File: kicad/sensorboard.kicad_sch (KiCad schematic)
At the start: 8 parts, among them J5 20021121-00010C4LF, U30 SHT40-AD1B-R2, U31 TMP117MAIDRVT

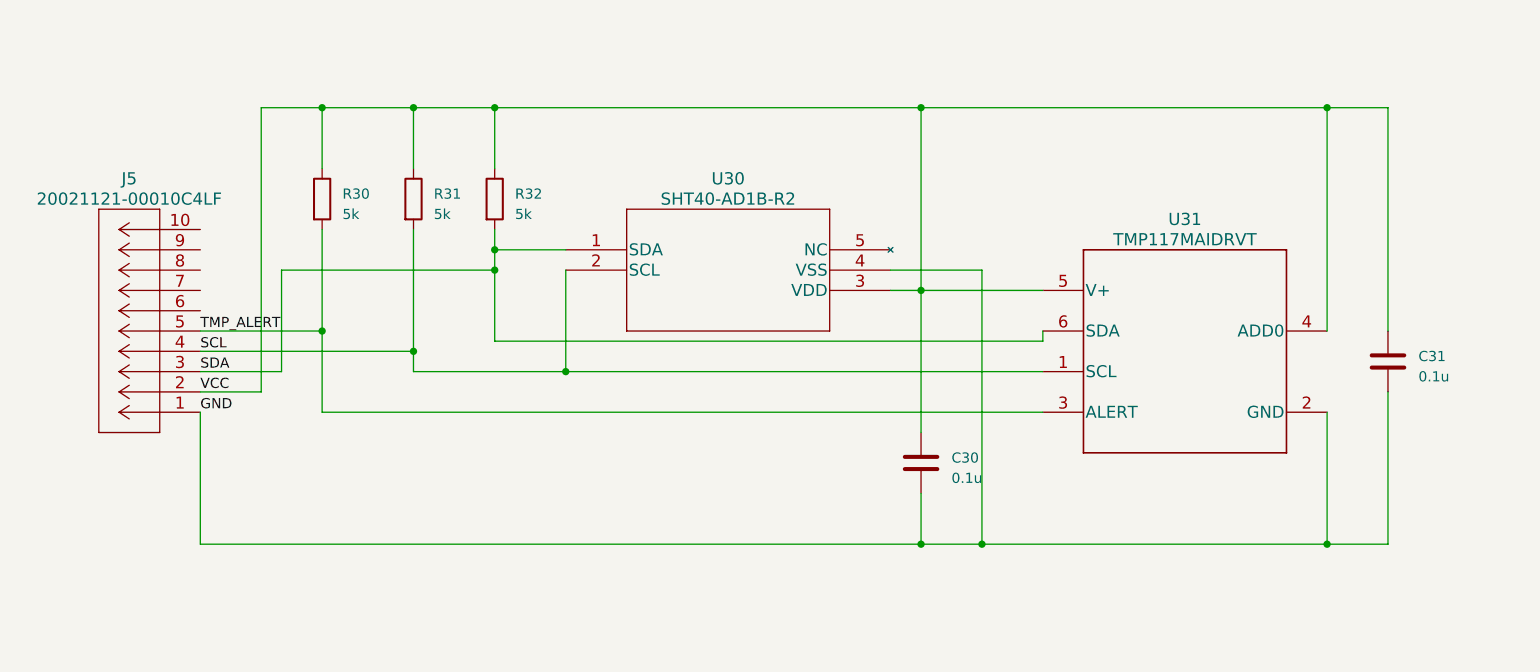
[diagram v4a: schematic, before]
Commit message: schematic editing, led selection
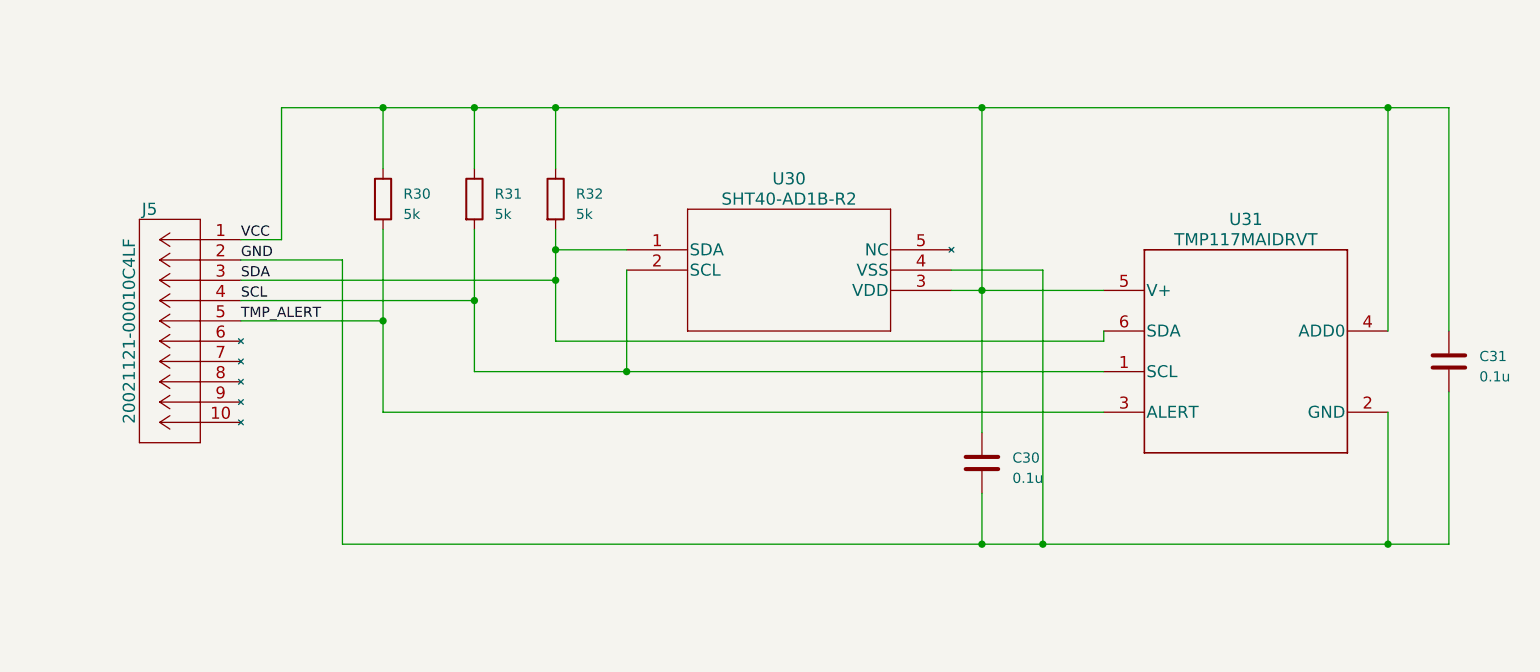
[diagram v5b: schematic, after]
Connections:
- net GND: now also J5.2; no longer J5.1
- net VCC: now also J5.1; no longer J5.2
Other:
- moved on the sheet: C30, C31, R30, R31, R32, U30, U31

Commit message: added footprints and Digikey codes
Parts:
- C30, C31: value 0.1u -> 100n; footprint (none) -> Capacitor_SMD:C_0603_1608Metric_Pad1.08x0.95mm_HandSolder; Digikey (none) -> 587-1245-1-ND
- R30, R31, R32: footprint (none) -> Resistor_SMD:R_0603_1608Metric_Pad0.98x0.95mm_HandSolder; Digikey (none) -> 13-RT0603BRE075KLCT-ND
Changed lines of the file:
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@@
       (effects (font (size 1.27 1.27)) (justify left))
     )
-    (property "Footprint" "" (at 49.022 43.18 90)
+    (property "Footprint" "Resistor_SMD:R_0603_1608Metric_Pad0.98x0.95mm_HandSolder" (at 49.022 43.18 90)
       (effects (font (size 1.27 1.27)) hide)
     )
     (property "Datasheet" "~" (at 50.8 43.18 0)
+      (effects (font (size 1.27 1.27)) hide)
+    )
+    (property "Digikey" "13-RT0603BRE075KLCT-ND" (at 50.8 43.18 0)
       (effects (font (size 1.27 1.27)) hide)
     )
@@
       (effects (font (size 1.27 1.27)) (justify left))
     )
-    (property "Value" "0.1u" (at 129.54 78.105 0)
+    (property "Value" "100n" (at 129.54 78.105 0)
       (effects (font (size 1.27 1.27)) (justify left))
     )
-    (property "Footprint" "" (at 126.6952 80.01 0)
+    (property "Footprint" "Capacitor_SMD:C_0603_1608Metric_Pad1.08x0.95mm_HandSolder" (at 126.6952 80.01 0)
       (effects (font (size 1.27 1.27)) hide)
     )
     (property "Datasheet" "~" (at 125.73 76.2 0)
+      (effects (font (size 1.27 1.27)) hide)
+    )
+    (property "Digikey" "587-1245-1-ND" (at 125.73 76.2 0)
       (effects (font (size 1.27 1.27)) hide)
     )
@@
       (effects (font (size 1.27 1.27)) (justify left))
     )
-    (property "Value" "0.1u" (at 187.96 65.405 0)
+    (property "Value" "100n" (at 187.96 65.405 0)
       (effects (font (size 1.27 1.27)) (justify left))
     )
-    (property "Footprint" "" (at 185.1152 67.31 0)
+    (property "Footprint" "Capacitor_SMD:C_0603_1608Metric_Pad1.08x0.95mm_HandSolder" (at 185.1152 67.31 0)
       (effects (font (size 1.27 1.27)) hide)
     )
     (property "Datasheet" "~" (at 184.15 63.5 0)
+      (effects (font (size 1.27 1.27)) hide)
+    )
+    (property "Digikey" "587-1245-1-ND" (at 184.15 63.5 0)
       (effects (font (size 1.27 1.27)) hide)
     )
@@
       (effects (font (size 1.27 1.27)) (justify left))
     )
-    (property "Footprint" "" (at 70.612 43.18 90)
+    (property "Footprint" "Resistor_SMD:R_0603_1608Metric_Pad0.98x0.95mm_HandSolder" (at 70.612 43.18 90)
       (effects (font (size 1.27 1.27)) hide)
     )
     (property "Datasheet" "~" (at 72.39 43.18 0)
+      (effects (font (size 1.27 1.27)) hide)
+    )
+    (property "Digikey" "13-RT0603BRE075KLCT-ND" (at 72.39 43.18 0)
       (effects (font (size 1.27 1.27)) hide)
     )
@@
       (effects (font (size 1.27 1.27)) (justify left))
     )
-    (property "Footprint" "" (at 60.452 43.18 90)
+    (property "Footprint" "Resistor_SMD:R_0603_1608Metric_Pad0.98x0.95mm_HandSolder" (at 60.452 43.18 90)
       (effects (font (size 1.27 1.27)) hide)
     )
@@
       (effects (font (size 1.27 1.27)) hide)
     )
+    (property "Digikey" "13-RT0603BRE075KLCT-ND" (at 62.23 43.18 0)
+      (effects (font (size 1.27 1.27)) hide)
+    )

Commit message: PCB update
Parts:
- J5: footprint CONN_00010C4LF_AMP -> 20021121-00010C4LF:20021121-00010C4LF; Digikey (none) -> 609-3695-1-ND
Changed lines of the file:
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@@
   (symbol (lib_id "20021121-00010C4LF:20021121-00010C4LF") (at 33.02 48.26 0) (mirror y) (unit 1)
     (in_bom yes) (on_board yes) (dnp no)
-    (property "Reference" "J5" (at 21.59 44.45 0)
+    (property "Reference" "J5" (at 44.45 44.45 0)
       (effects (font (size 1.524 1.524)))
     )
-    (property "Value" "20021121-00010C4LF" (at 19.05 59.69 90)
+    (property "Value" "20021121-00010C4LF" (at 46.99 59.69 90)
       (effects (font (size 1.524 1.524)))
     )
-    (property "Footprint" "CONN_00010C4LF_AMP" (at 43.18 59.944 0)
+    (property "Footprint" "20021121-00010C4LF:20021121-00010C4LF" (at 22.86 59.944 0)
       (effects (font (size 1.524 1.524)) hide)
     )
@@
       (effects (font (size 1.524 1.524)))
     )
+    (property "Digikey" "609-3695-1-ND" (at 33.02 48.26 0)
+      (effects (font (size 1.27 1.27)) hide)
+    )
     (pin "1")
